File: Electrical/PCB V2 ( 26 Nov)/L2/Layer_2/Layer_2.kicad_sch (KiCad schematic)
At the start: 26 parts, among them J1 Conn_01x02, SW1 SW_Push, U1 LM2596ADJ, U10 L298N, U11 XT30UPB-M, U2 LM2596ADJ, U3 XT30UPB-M, U4 XT30UPB-M, U5 ESP32-S3-DEVKITM-1-N8, U6 XT30UPB-M, U7 XT30UPB-M, U8 L298N, U9 XT30UPB-M

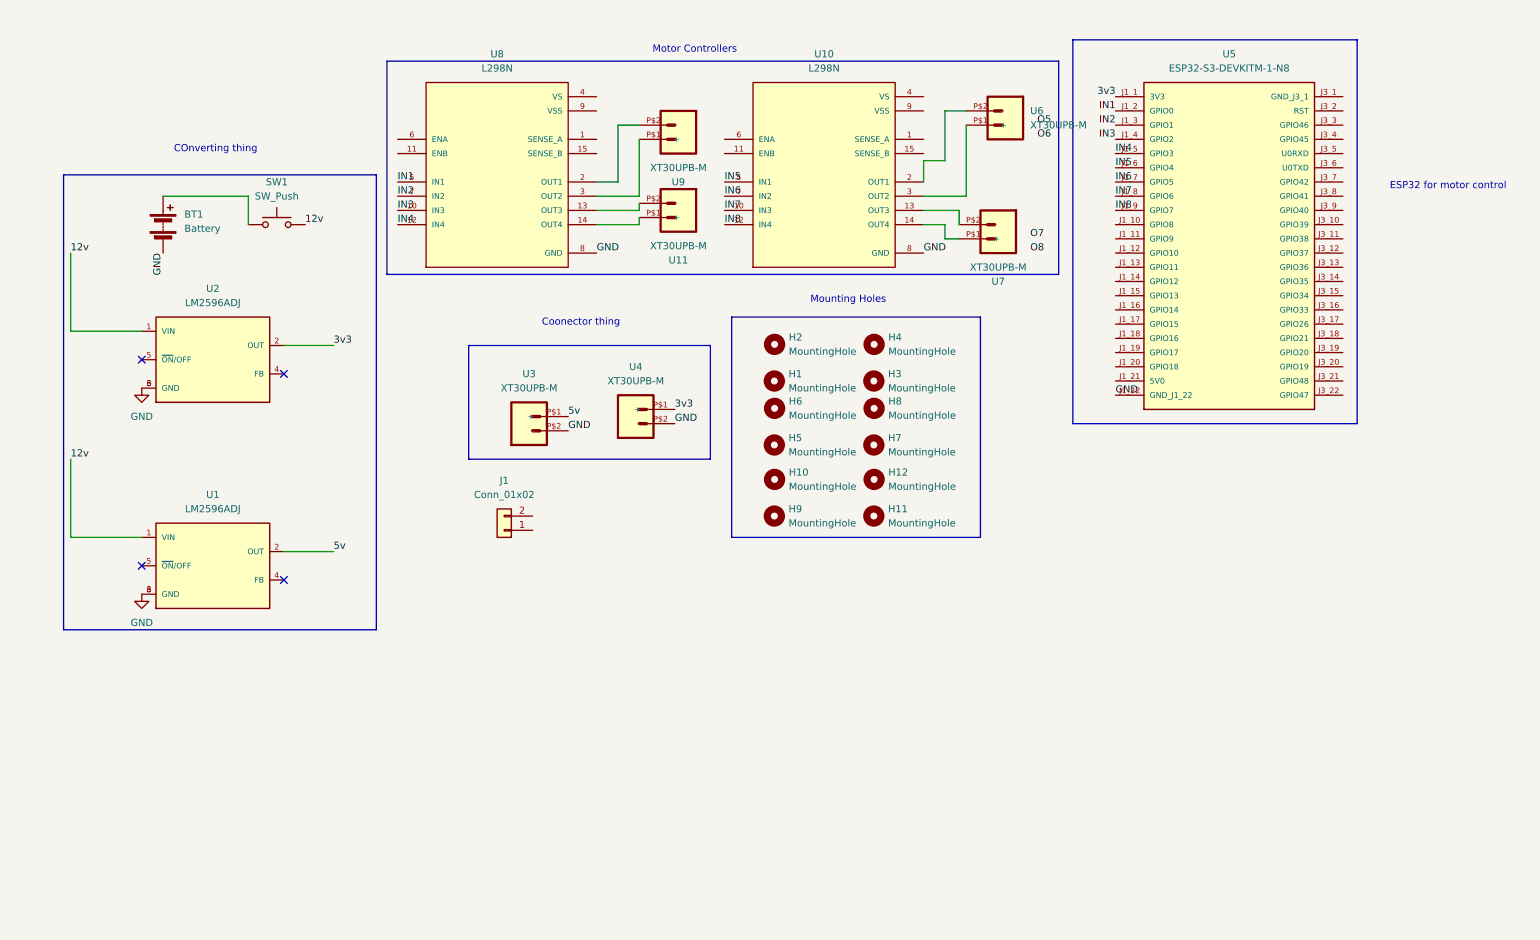
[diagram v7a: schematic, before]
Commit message: motor driver for motor 1 done
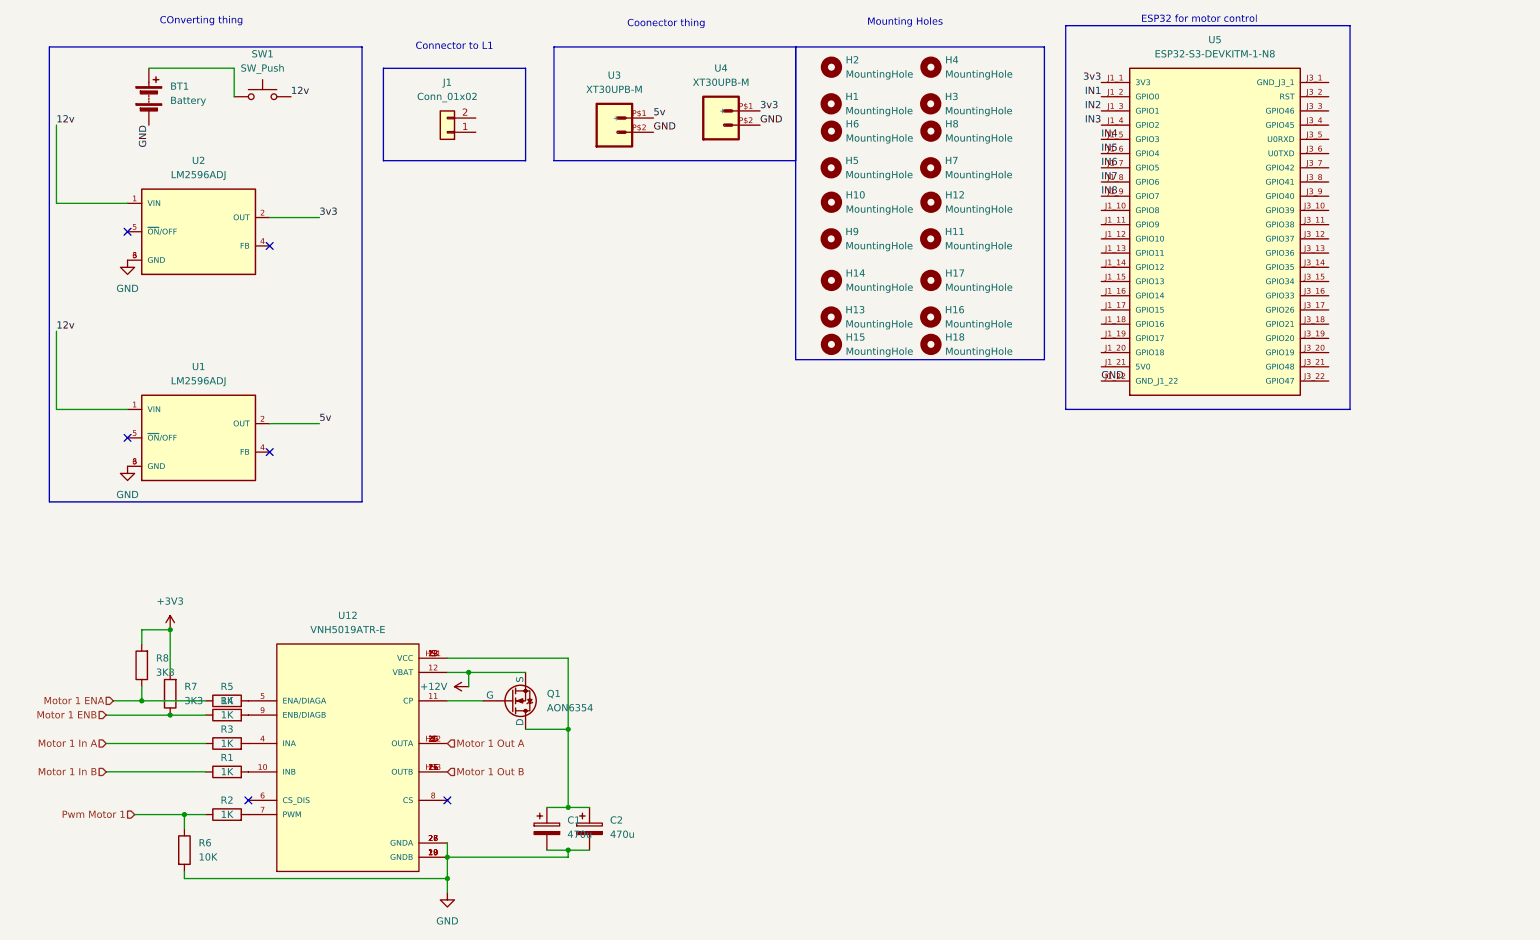
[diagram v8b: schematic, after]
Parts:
- removed U10, U8: L298N, L298N:TO127P2020X500X2100-15, symbol l298n:L298N
- removed U11, U6, U7, U9: XT30UPB-M, xt30:XT30UPB-M, symbol XT30UPB-M:XT30UPB-M
- added C1, C2: 470u, 2024l2:CP_Radial_D8.0mm_P3.50mm, symbol Device:C_Polarized
- added H13, H14, H15, H16, H17, H18: MountingHole, MountingHole:MountingHole_3.2mm_M3_DIN965_Pad, symbol Mechanical:MountingHole
- added Q1: AON6354, 2024l2:8-DFN (5x6), symbol vincent:AON6354
- added R1, R2, R3, R4, R5: 1K, 2024l2:res0603, symbol Device:R
- added R6: 10K, 2024l2:res0603, symbol Device:R
- added R7, R8: 3K3, 2024l2:res0603, symbol Device:R
- added U12: VNH5019ATR-E, VNH5019ATR-E:IC_VNH5019ATR-E, symbol VHN5019ATR-E:VNH5019ATR-E
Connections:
- net GND: now also C1.2, C2.2, R6.2, U12.18 (GNDB), U12.19 (GNDB), U12.20 (GNDB), U12.26 (GNDA), U12.27 (GNDA), U12.28 (GNDA)
- new net: R2.2, U12.7 (PWM)
- new net: R3.2, U12.4 (INA)
- new net: C1.1, C2.1, Q1.5 (D), Q1.6 (D), Q1.7 (D), Q1.8 (D), Q1.9 (D), U12.13 (VCC), U12.23 (VCC), U12.3 (VCC), U12.HS1 (VCC)
- new net: R4.2, U12.9 (ENB/DIAGB)
- new net: R5.2, U12.5 (ENA/DIAGA)
- new net: Q1.4 (G), U12.11 (CP)
- new net: R1.2, U12.10 (INB)
- new net +12V: Q1.1 (S), Q1.2 (S), Q1.3 (S), U12.12 (VBAT)
- new net +3V3: R7.2, R8.2
- new net Motor 1 ENA: R5.1, R8.1
- new net Motor 1 ENB: R4.1, R7.1
- new net Motor 1 In A: R3.1
- new net Motor 1 In B: R1.1
- new net Motor 1 Out A: U12.1 (OUTA), U12.25 (OUTA), U12.30 (OUTA), U12.HS2 (OUTA)
- new net Motor 1 Out B: U12.15 (OUTB), U12.16 (OUTB), U12.21 (OUTB), U12.HS3 (OUTB)
- new net Pwm Motor 1: R2.1, R6.1
- no-connect marks 4 -> 6
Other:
- note added: "Connector to L1"
- note removed: "Motor Controllers"
- moved on the sheet: BT1, H1, H10, H11, H12, H2, H3, H4, H5, H6, H7, H8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
